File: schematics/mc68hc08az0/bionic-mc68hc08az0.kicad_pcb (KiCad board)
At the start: 2 copper layers, 25.4 x 68.6 mm, 12 parts, among them J1 Bionic-P135, J2 Bionic-P245, U1 MC68HC08AZ0, U2 11AA010-I/TT

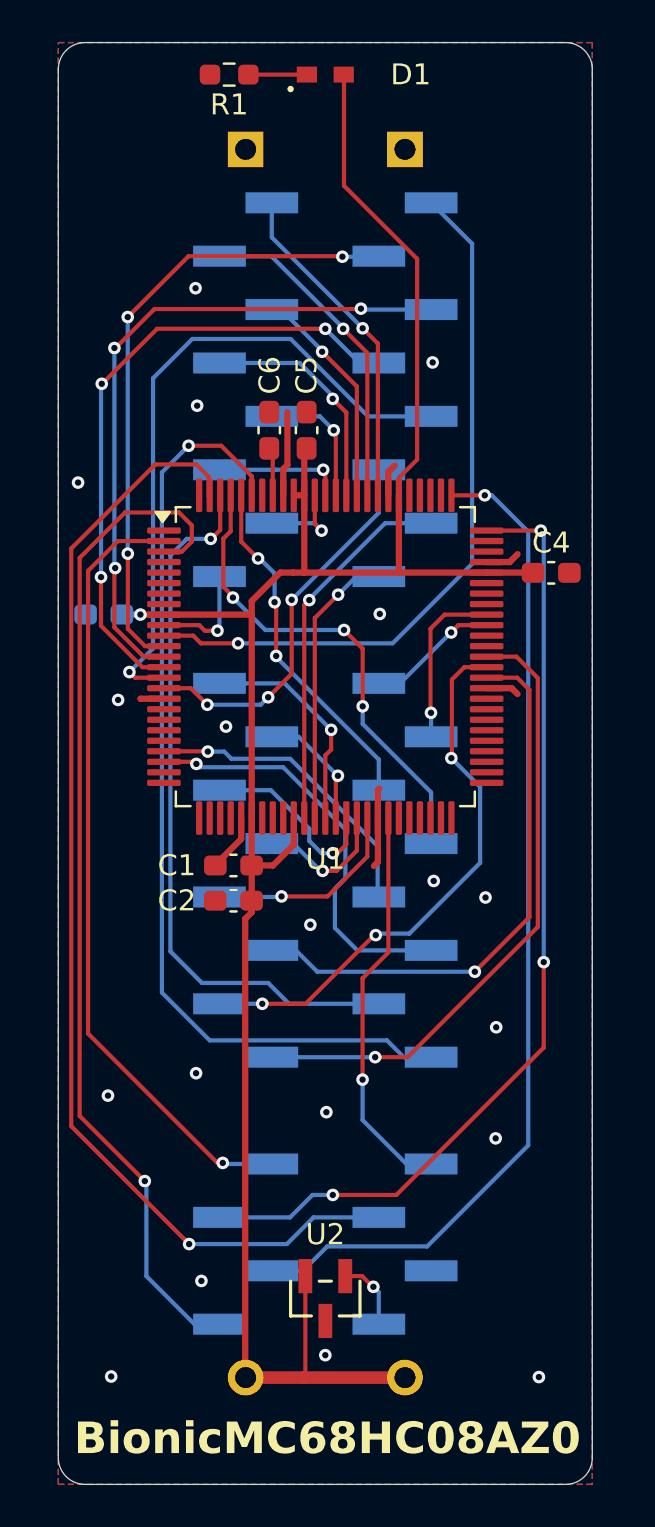
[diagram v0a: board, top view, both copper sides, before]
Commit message: [schematics] Straighten board tracks and regenerate Gerbers
straighten_tracks.py on every routed board: router leftovers snapped to
0/45/90 degrees and redundant segments merged, each pass DRC-checked
(counts unchanged). Gerbers and drill files of the changed boards are
regenerated with each board's plot settings, keeping the committed file
sets; tms9980 keeps its tracks (the rebuild left a dangling VCC stub).
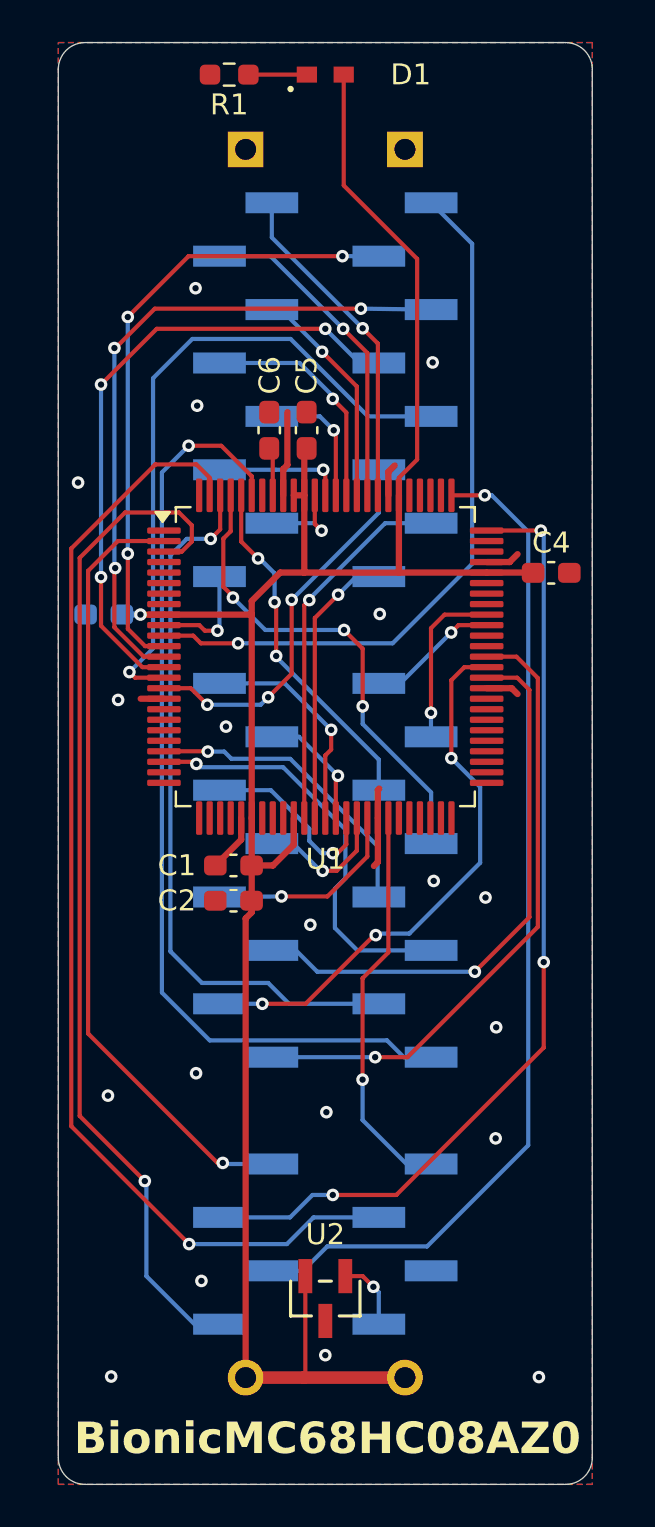
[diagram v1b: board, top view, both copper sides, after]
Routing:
- net /P53: track 48.7 -> 47.5 mm
- net /P54: track 19.0 -> 17.8 mm
- net /P35: track 26.8 -> 25.7 mm
- net /P27: track 13.4 -> 12.3 mm
- net /P33: track 6.53 -> 5.51 mm
- net /P40: track 6.28 -> 5.26 mm
- net /P23: track 30.3 -> 29.4 mm

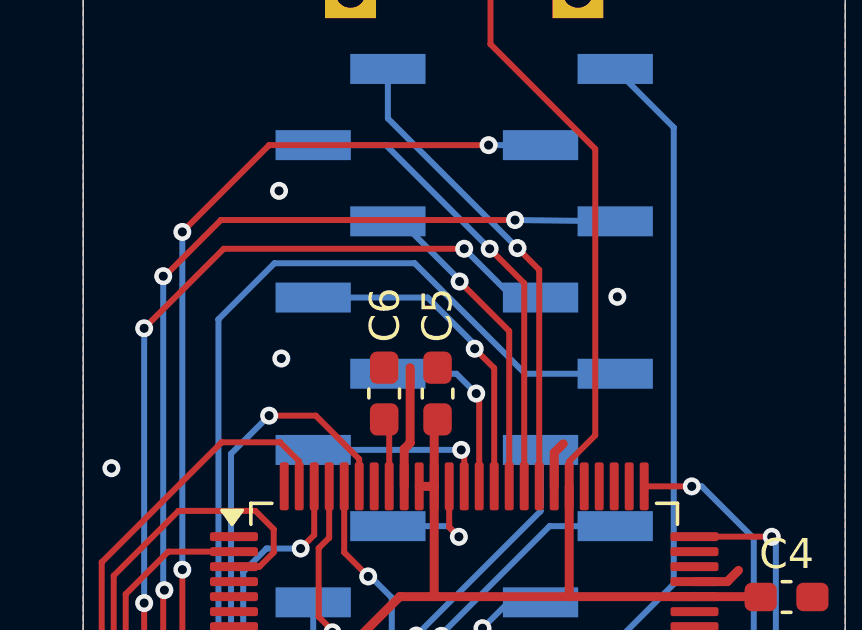
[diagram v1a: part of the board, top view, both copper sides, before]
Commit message: [schematics] Align silkscreen reference labels
align_silk.py snaps each footprint kind's labels onto their common
offset and angle and clears labels DRC flags on silkscreen; 76 labels on
22 boards, no DRC count grows. Their Gerbers are regenerated.
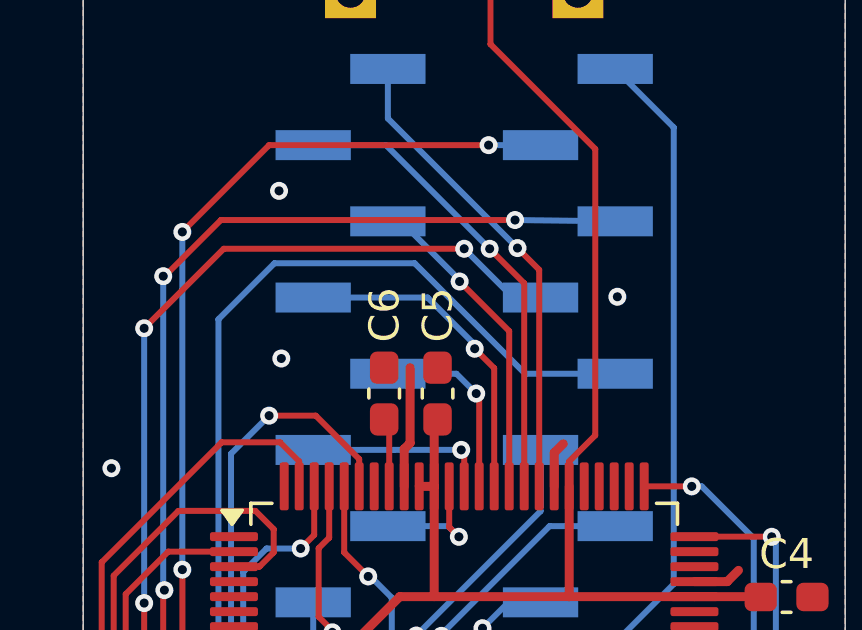
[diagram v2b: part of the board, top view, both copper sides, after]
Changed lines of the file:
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@@
 		(tags "capacitor handsolder")
 		(property "Reference" "C6"
-			(at 2.6173 0.0254 90)
+			(at 2.62 0.01 90)
 			(layer "F.SilkS")
 			(effects
@@
 		(tags "capacitor handsolder")
 		(property "Reference" "C5"
-			(at 2.6162 0 90)
-			(layer "F.SilkS")
-			(effects
+			(at 2.62 0.01 90)
+			(layer "F.SilkS")
+			(effects

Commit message: [schematics] Remove the JLC order-number marker from all boards
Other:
- board text removed: "JLCJLCJLCJLC"
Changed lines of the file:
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@@
-		)
-	)
-	(gr_text "JLCJLCJLCJLC"
-		(at 88.9 143.3576 0)
-		(layer "B.SilkS")
-		(effects
-			(font
-				(size 0.8 0.8)
-				(thickness 0.1)
-			)
-			(justify bottom mirror)
 		)
 	)
